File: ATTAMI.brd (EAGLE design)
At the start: 22.8 x 22.9 mm, 19 parts, among them J1 CON_HEADER_1X02-PTH, J2 MICRO-USB_ALIEXPRESS, J3 CON_HEADER_1X02-PTH, U1 MIC5225, U2 ATTINY85

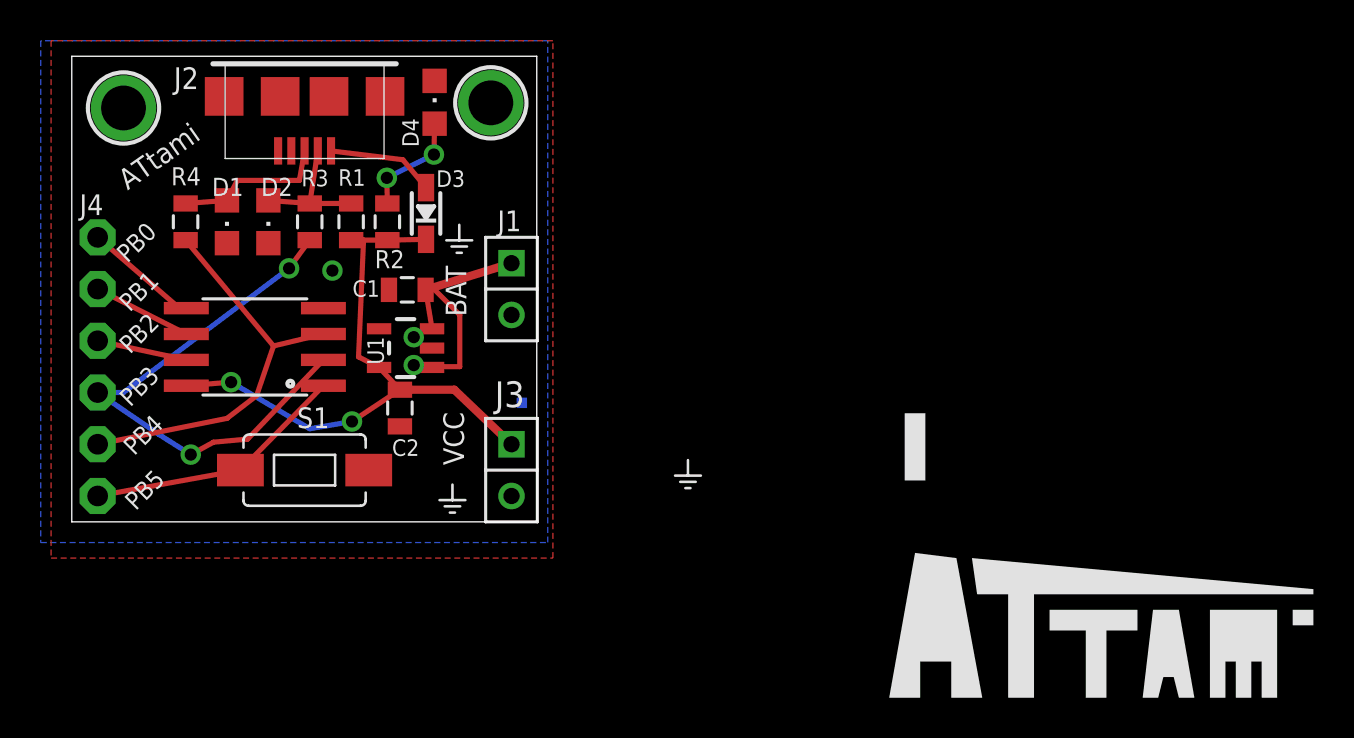
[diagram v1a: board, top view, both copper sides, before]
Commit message: ver 15c
curved and fixed overlaps
used DRU rules by OSHpark
https://oshpark.com/guidelines
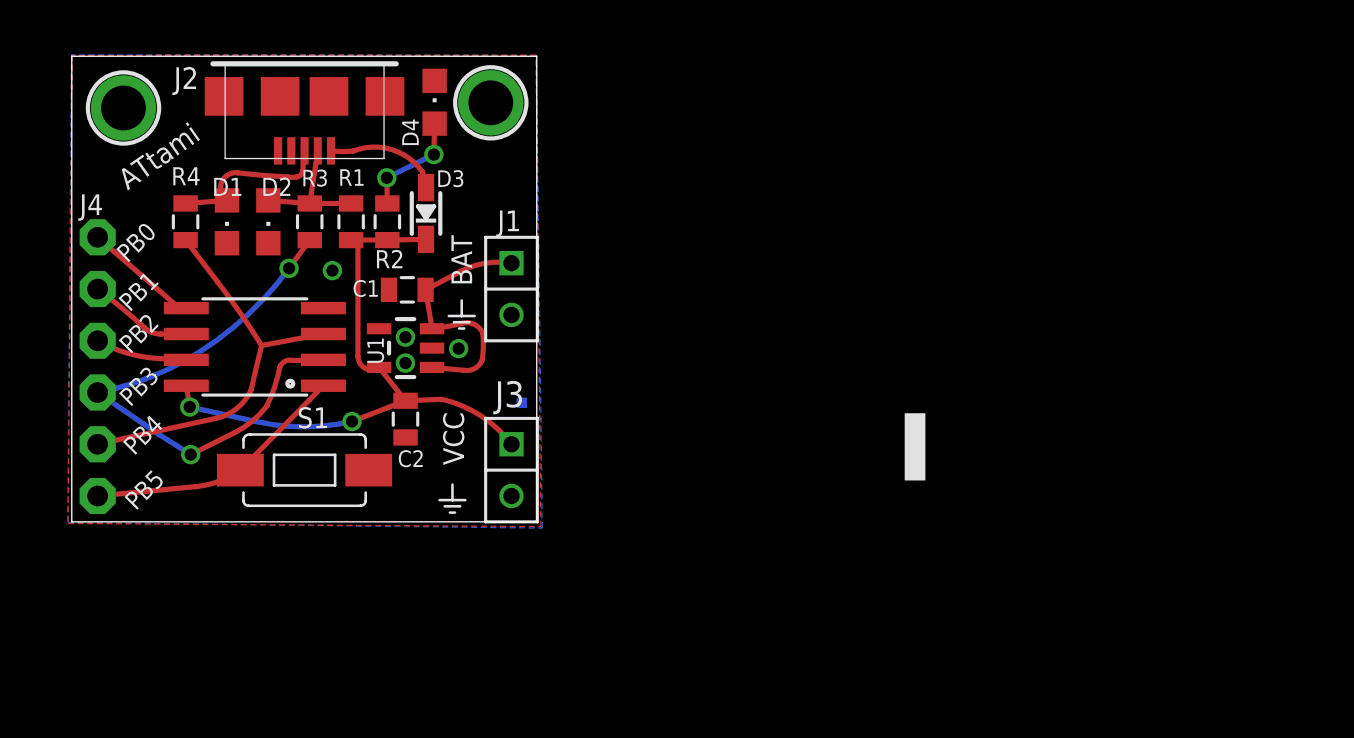
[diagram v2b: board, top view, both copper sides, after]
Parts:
- moved C2 0.61 mm to (16.4, 5.04)
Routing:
- net V_BAT: track 12.1 -> 12.9 mm
